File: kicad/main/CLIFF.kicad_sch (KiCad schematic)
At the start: 9 parts, among them Q6 2302V

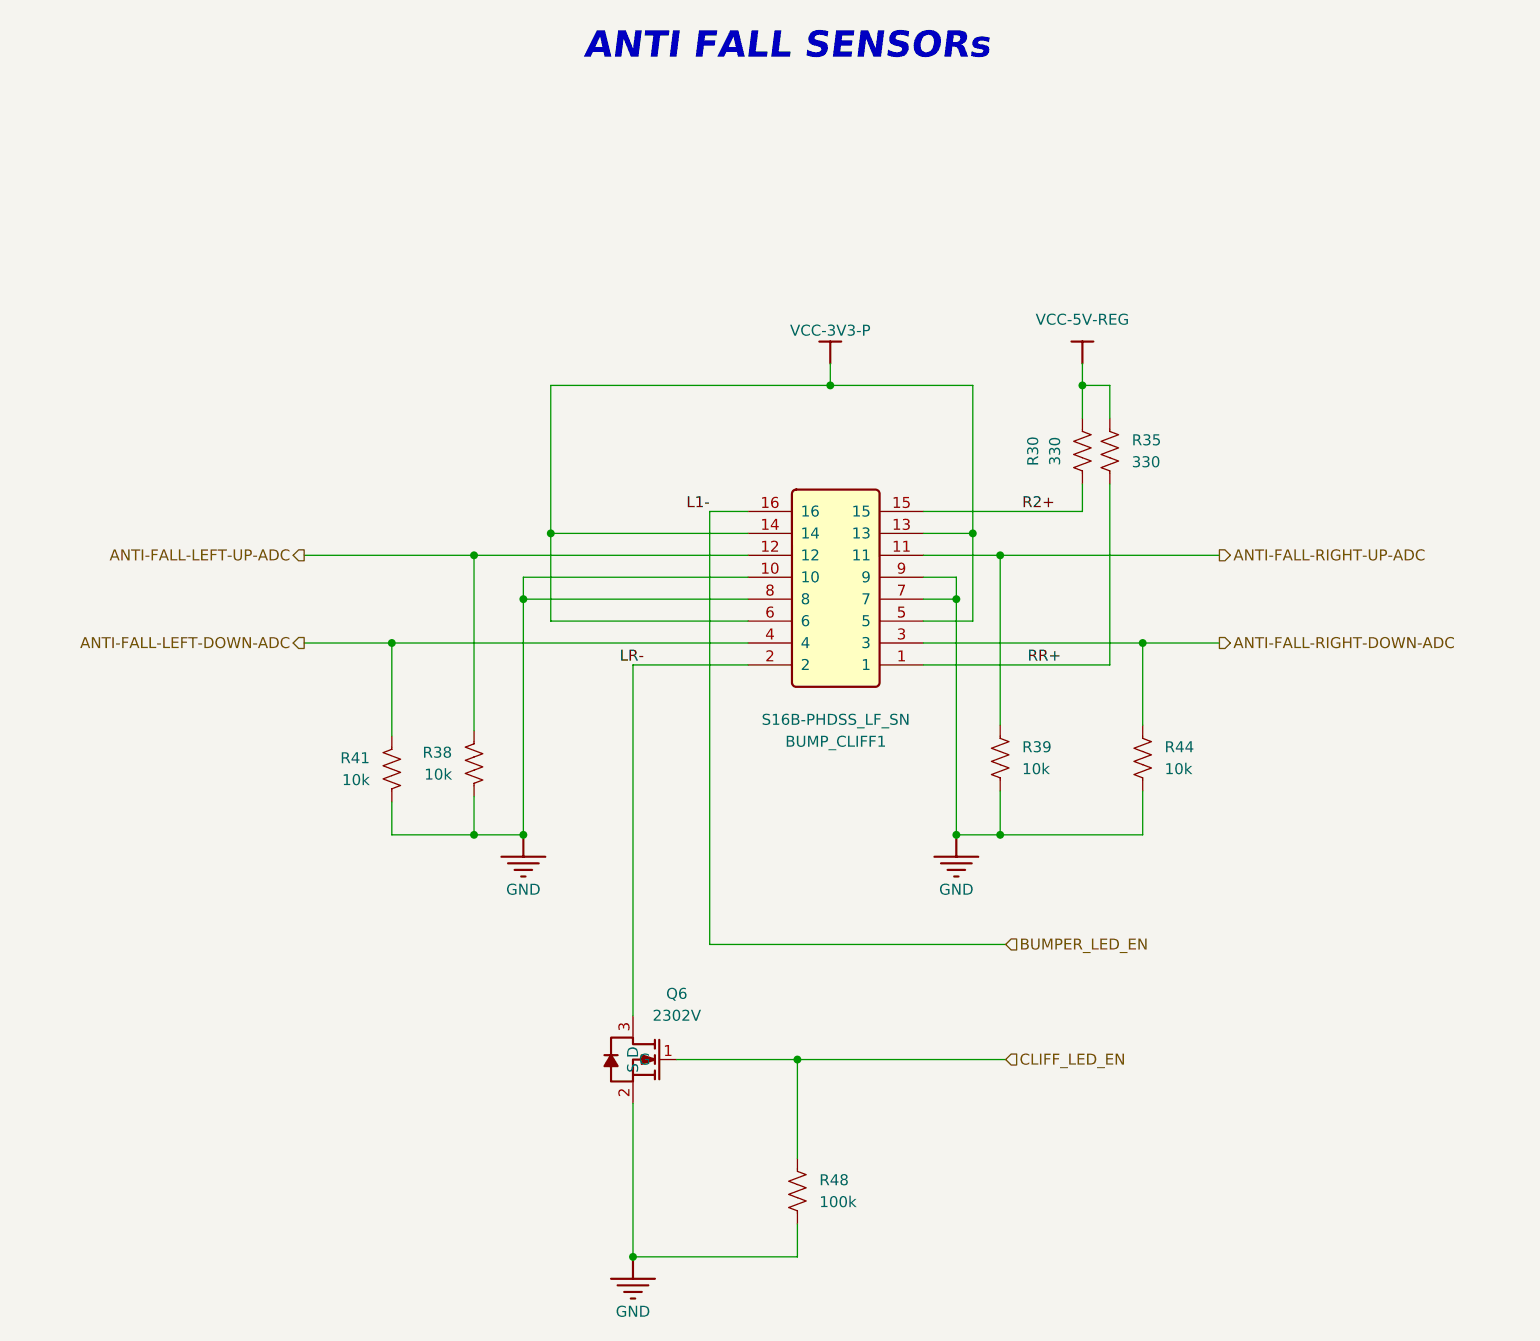
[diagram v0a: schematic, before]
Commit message: Cliff/bumper connector reverse engineered
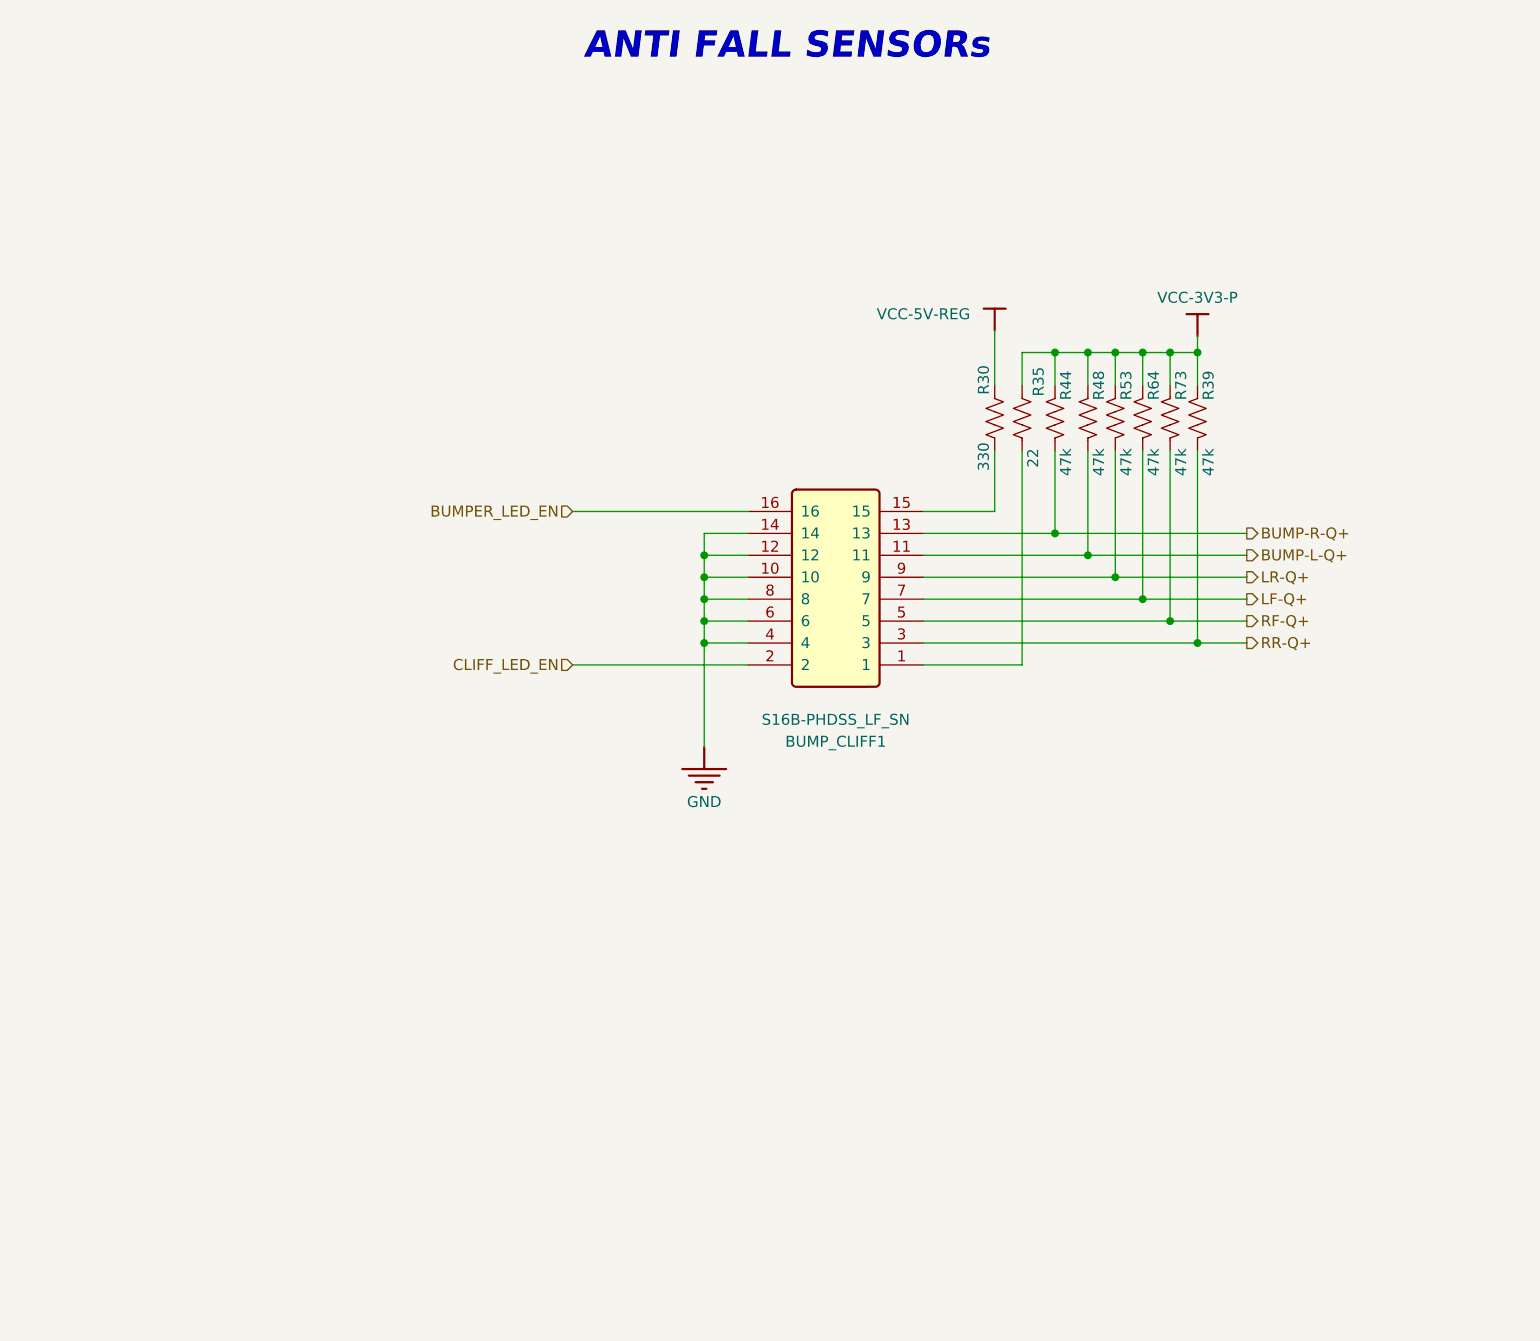
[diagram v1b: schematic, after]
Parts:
- removed Q6: 2302V, JLCImport:2302V, symbol JLCImport:2302V
- removed R38, R41: 10k, Resistor_SMD:R_0603_1608Metric, symbol Device:R_US
- added R53, R64, R73: 47k, Resistor_SMD:R_0603_1608Metric, symbol Device:R_US
- R35: value 330 -> 22
- R39, R44: value 10k -> 47k
- R48: value 100k -> 47k
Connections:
- net ANTI-FALL-LEFT-DOWN-ADC is gone; now on net GND: BUMP_CLIFF1.4
- net ANTI-FALL-LEFT-UP-ADC is gone; now on net GND: BUMP_CLIFF1.12
- net LR- is gone; now on net CLIFF_LED_EN: BUMP_CLIFF1.2
- net CLIFF_LED_EN: no longer R48.1
- net GND: now also BUMP_CLIFF1.14, BUMP_CLIFF1.6; no longer BUMP_CLIFF1.7, BUMP_CLIFF1.9, R39.2, R44.2, R48.2
- net VCC-3V3-P: now also R35.2, R39.2, R44.2, R48.2, R53.2, R64.2, R73.2; no longer BUMP_CLIFF1.13, BUMP_CLIFF1.14, BUMP_CLIFF1.5, BUMP_CLIFF1.6
- net VCC-5V-REG: no longer R35.2
- net ANTI-FALL-RIGHT-DOWN-ADC renamed BUMP-R-Q+
- net BUMP-R-Q+: now also BUMP_CLIFF1.13; no longer BUMP_CLIFF1.3
- net ANTI-FALL-RIGHT-UP-ADC renamed BUMP-L-Q+
- net BUMP-L-Q+: now also R48.1; no longer R39.1
- net R2+: no longer names the net of BUMP_CLIFF1.15, R30.1
- net RR+: no longer names the net of BUMP_CLIFF1.1, R35.1
- new net LF-Q+: BUMP_CLIFF1.7, R64.1
- new net LR-Q+: BUMP_CLIFF1.9, R53.1
- new net RF-Q+: BUMP_CLIFF1.5, R73.1
- new net RR-Q+: BUMP_CLIFF1.3, R39.1
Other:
- moved on the sheet: R30, R35

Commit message: STM32 power rail switch
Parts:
- R30: LCSC (none) -> C2907152
- R35: LCSC (none) -> C23345
- R39, R44, R48, R53, R64, R73: LCSC (none) -> C2907042
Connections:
- net VCC-3V3-P renamed VCC-3V3-REG
